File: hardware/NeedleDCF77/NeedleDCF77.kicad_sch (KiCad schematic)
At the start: 72 parts, among them J1 USB_C_Receptacle_USB2.0

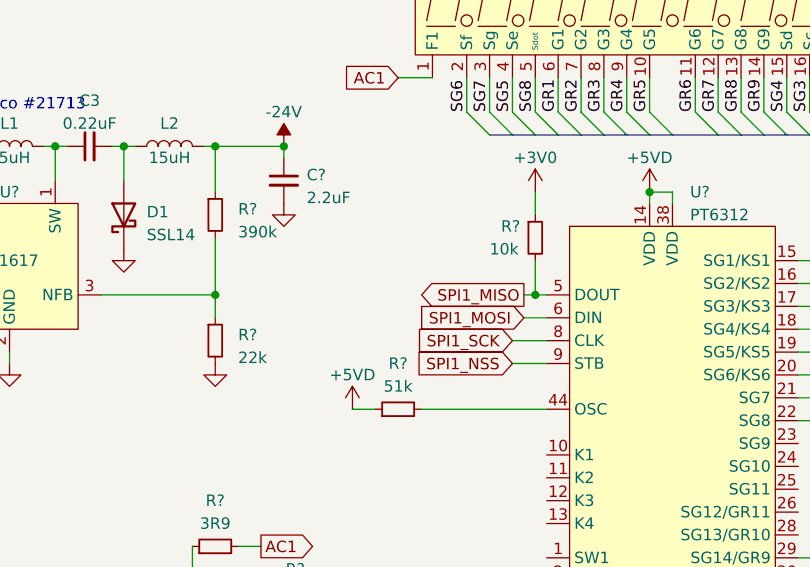
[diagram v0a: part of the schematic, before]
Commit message: Add solder jumper between Dout and Din for PT6312
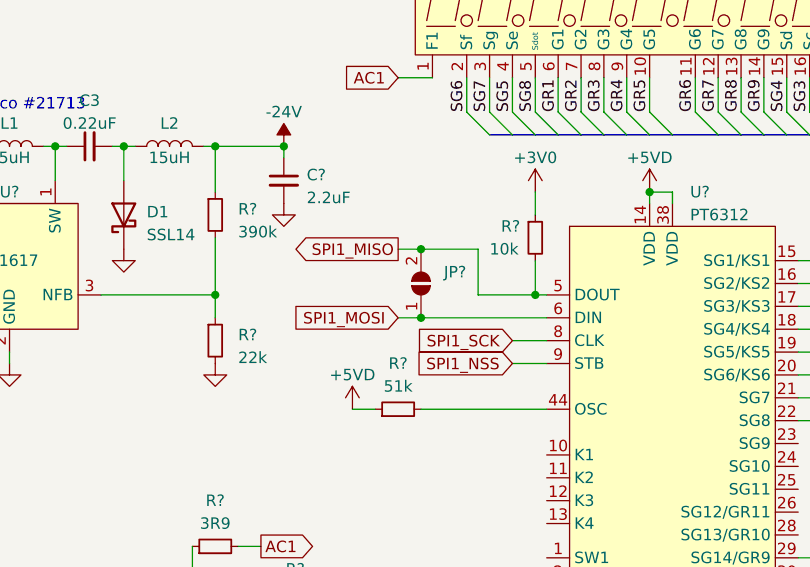
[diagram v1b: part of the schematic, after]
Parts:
- added JP?: (no value), symbol Jumper:SolderJumper_2_Open
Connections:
- net SPI1_MISO: now also JP?.2 (B)
- net SPI1_MOSI: now also JP?.1 (A)
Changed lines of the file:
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@@
   (junction (at 60.96 133.35) (diameter 0) (color 0 0 0 0)
   )
+  (junction (at 96.52 133.35) (diameter 0) (color 0 0 0 0)
+  )
   (junction (at 189.23 36.83) (diameter 0) (color 0 0 0 0)
   )
@@
   (junction (at 147.32 62.23) (diameter 0) (color 0 0 0 0)
   )
-  (junction (at 96.52 133.35) (diameter 0) (color 0 0 0 0)
-  )
   (junction (at 284.48 113.03) (diameter 0) (color 0 0 0 0)
   )
@@
   (junction (at 255.27 58.42) (diameter 0) (color 0 0 0 0)
   )
+  (junction (at 83.82 128.27) (diameter 0) (color 0 0 0 0)
+  )
   (junction (at 203.2 71.12) (diameter 0) (color 0 0 0 0)
   )
@@
   (junction (at 34.29 116.84) (diameter 0) (color 0 0 0 0)
   )
+  (junction (at 83.82 135.89) (diameter 0) (color 0 0 0 0)
+  )
   (junction (at 58.42 185.42) (diameter 0) (color 0 0 0 0)
   )
@@
     (stroke (width 0) (type default))
   )
+  (wire (pts (xy 90.17 128.27) (xy 90.17 133.35))
+    (stroke (width 0) (type default))
+  )
   (wire (pts (xy 284.48 110.49) (xy 284.48 113.03))
     (stroke (width 0) (type default))
@@
     (stroke (width 0) (type default))
   )
+  (wire (pts (xy 81.28 128.27) (xy 83.82 128.27))
+    (stroke (width 0) (type default))
+  )
   (wire (pts (xy 299.72 74.93) (xy 303.53 74.93))
     (stroke (width 0) (type default))
@@
     (stroke (width 0) (type default))
   )
-  (wire (pts (xy 95.25 133.35) (xy 96.52 133.35))
-    (stroke (width 0) (type default))
-  )
   (wire (pts (xy 147.32 62.23) (xy 152.4 62.23))
     (stroke (width 0) (type default))
@@
     (stroke (width 0) (type default))
   )
-  (wire (pts (xy 95.25 135.89) (xy 97.79 135.89))
+  (wire (pts (xy 81.28 135.89) (xy 83.82 135.89))
     (stroke (width 0) (type default))
   )
@@
     (stroke (width 0) (type default))
   )
+  (wire (pts (xy 83.82 135.89) (xy 97.79 135.89))
+    (stroke (width 0) (type default))
+  )
   (wire (pts (xy 111.76 123.19) (xy 111.76 121.92))
     (stroke (width 0) (type default))
@@
     (stroke (width 0) (type default))
   )
+  (wire (pts (xy 90.17 133.35) (xy 96.52 133.35))
+    (stroke (width 0) (type default))
+  )
   (wire (pts (xy 22.86 189.23) (xy 22.86 186.69))
     (stroke (width 0) (type default))
@@
     (stroke (width 0) (type default))
   )
+  (wire (pts (xy 83.82 128.27) (xy 90.17 128.27))
+    (stroke (width 0) (type default))
+  )
   (wire (pts (xy 152.4 41.91) (xy 128.27 41.91))
     (stroke (width 0) (type default))
@@
     )
   )
-  (global_label "SPI1_MOSI" (shape input) (at 95.25 135.89 180) (fields_autoplaced)
+  (global_label "SPI1_MOSI" (shape input) (at 81.28 135.89 180) (fields_autoplaced)
     (effects (font (size 1.27 1.27)) (justify right))
-    (property "Intersheetrefs" "${INTERSHEET_REFS}" (at 82.4866 135.89 0)
+    (property "Intersheetrefs" "${INTERSHEET_REFS}" (at 68.5166 135.89 0)
       (effects (font (size 1.27 1.27)) (justify right) hide)
     )
@@
     )
   )
-  (global_label "SPI1_MISO" (shape output) (at 95.25 133.35 180) (fields_autoplaced)
+  (global_label "SPI1_MISO" (shape output) (at 81.28 128.27 180) (fields_autoplaced)
     (effects (font (size 1.27 1.27)) (justify right))
-    (property "Intersheetrefs" "${INTERSHEET_REFS}" (at 82.4866 133.35 0)
+    (property "Intersheetrefs" "${INTERSHEET_REFS}" (at 68.5166 128.27 0)
       (effects (font (size 1.27 1.27)) (justify right) hide)
     )
@@
         )
       )
+    )
+  )
+  (symbol (lib_id "Jumper:SolderJumper_2_Open") (at 83.82 132.08 90) (unit 1)
+    (in_bom yes) (on_board yes) (dnp no)
+    (property "Reference" "JP?" (at 86.36 130.81 90)
+      (effects (font (size 1.27 1.27)) (justify right))
+    )
+    (property "Value" "" (at 72.39 132.08 90)
+      (effects (font (size 1.27 1.27)) (justify right))
+    )
+    (property "Footprint" "" (at 83.82 132.08 0)
+      (effects (font (size 1.27 1.27)) hide)
+    )
+    (property "Datasheet" "~" (at 83.82 132.08 0)
+      (effects (font (size 1.27 1.27)) hide)
+    )
+    (pin "1")
+    (pin "2")
+    (instances
+      (project "NeedleDCF77"
+        (path "/9538e4ed-27e6-4c37-b989-9859dc0d49e8"
+          (reference "JP?") (unit 1)
+        )
+      )

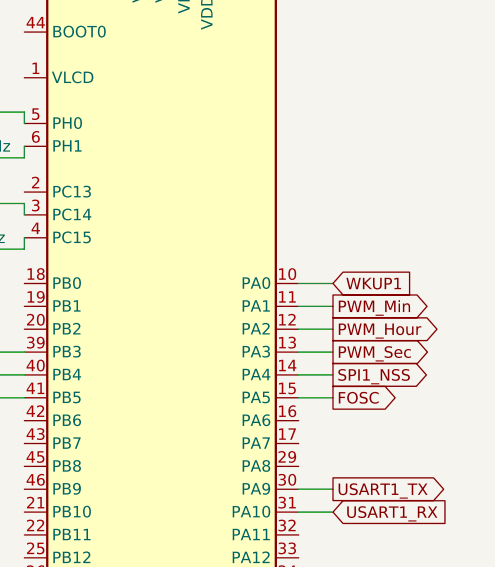
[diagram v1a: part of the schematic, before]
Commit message: Change WKUP to EXTI0, so we are unable to get out of LowPower modes, no STOP
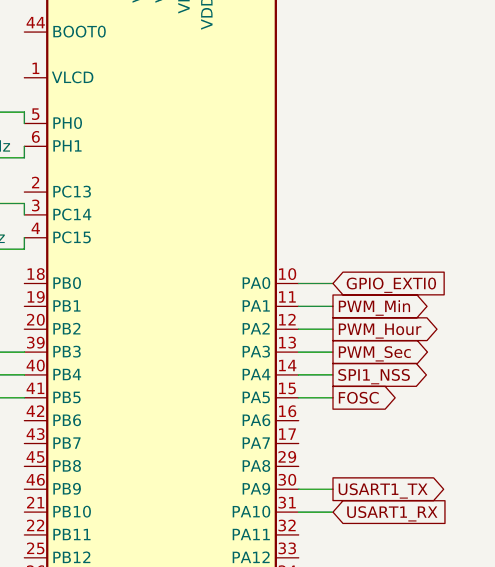
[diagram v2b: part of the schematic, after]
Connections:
- net WKUP1 renamed GPIO_EXTI0
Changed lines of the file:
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@@
     )
   )
-  (global_label "WKUP1" (shape input) (at 303.53 67.31 0) (fields_autoplaced)
+  (global_label "GPIO_EXTI0" (shape input) (at 303.53 67.31 0) (fields_autoplaced)
     (effects (font (size 1.27 1.27)) (justify left))
-    (property "Intersheetrefs" "${INTERSHEET_REFS}" (at 312.4745 67.2306 0)
+    (property "Intersheetrefs" "${INTERSHEET_REFS}" (at 317.0191 67.31 0)
       (effects (font (size 1.27 1.27)) (justify left) hide)
     )

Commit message: Add debug interfaces
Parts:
- added D?: CD4148W, Diode_SMD:D_0805_2012Metric, symbol Diode:CD4148W
- added J?: UART, symbol Connector:Conn_01x03_Pin
- added J?: DSW, symbol Connector:Conn_01x04_Pin
- JP?: value (none) -> ~
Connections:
- net +3V0: now also D?.1 (K)
- net GND: now also J?.1 (Pin_1), J?.3 (Pin_3)
- net SWCLK: now also J?.2 (Pin_2)
- net SWDIO: now also J?.3 (Pin_3)
- net USART1_RX: now also J?.1 (Pin_1)
- net USART1_TX: now also J?.2 (Pin_2)
- new net: D?.2 (A), J?.4 (Pin_4)
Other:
- moved on the sheet: C?, J?, JP?, R?, RV?, U?, VFD?

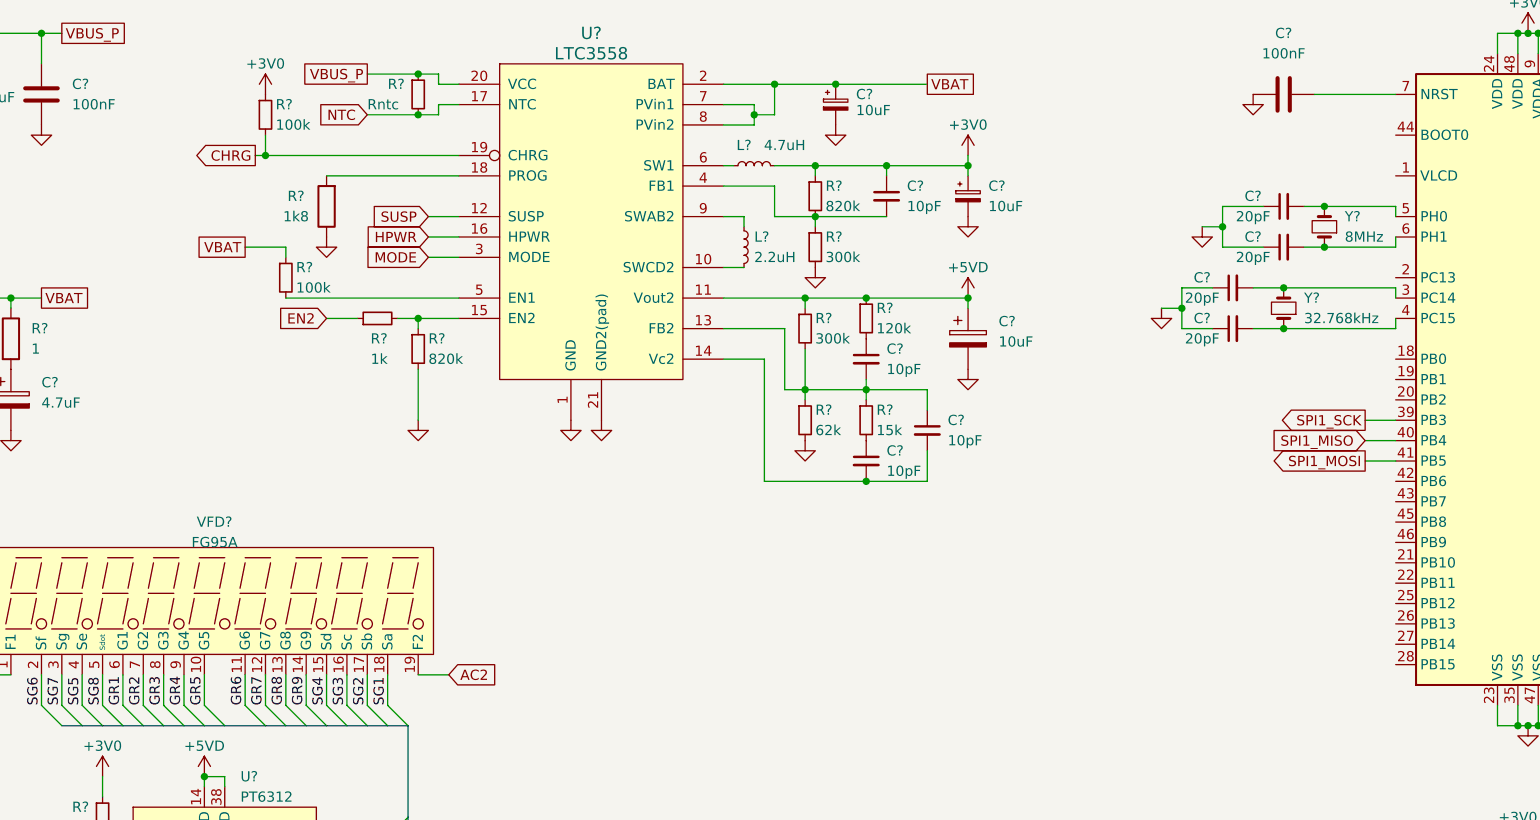
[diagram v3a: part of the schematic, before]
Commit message: Connect LTC3558 logic to MCU
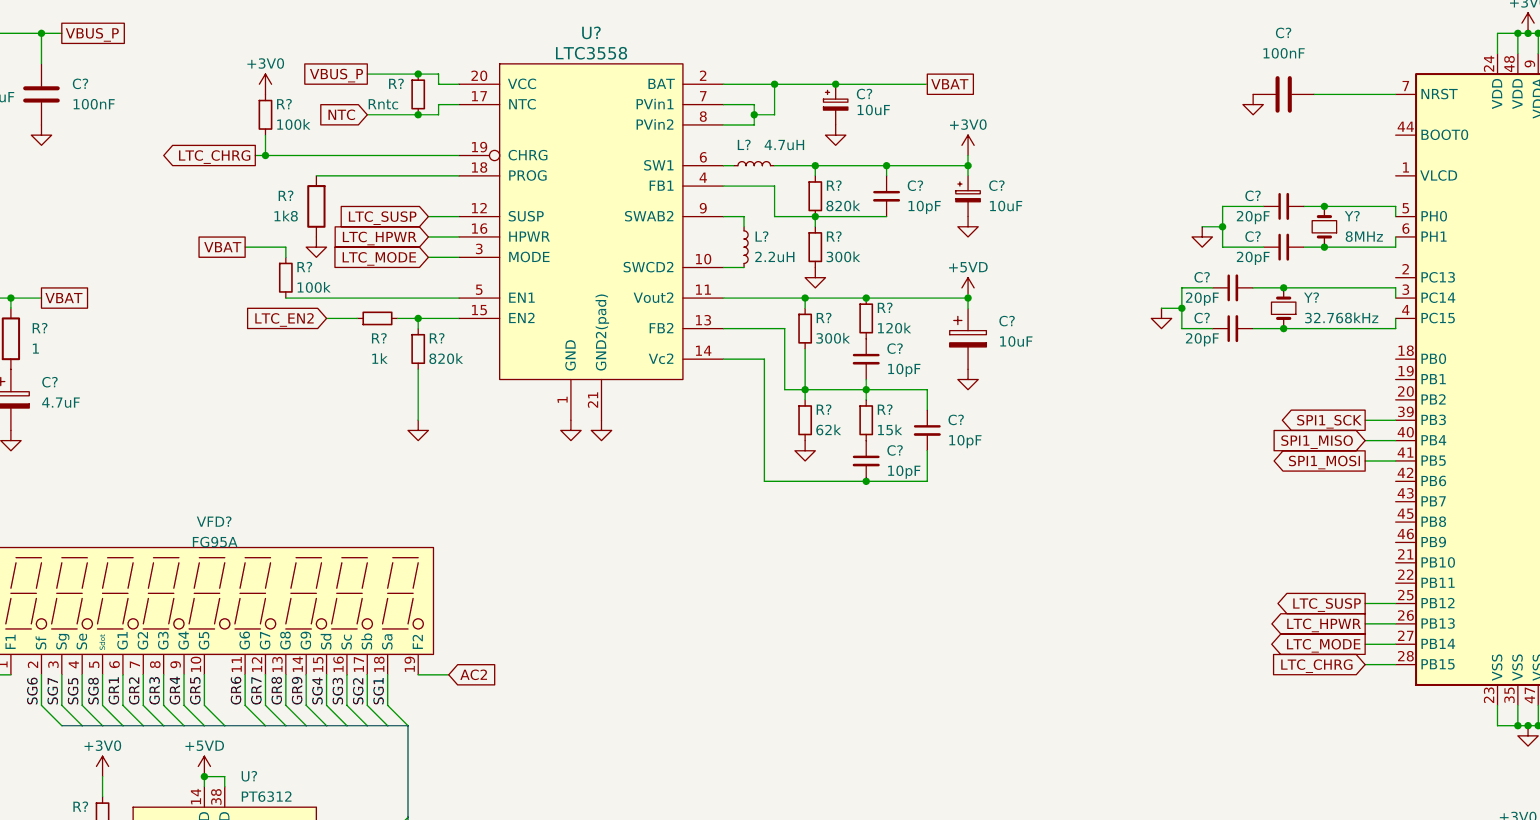
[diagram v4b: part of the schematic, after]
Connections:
- net CHRG is gone; now on net LTC_CHRG: R?.2, U?.19 (CHRG)
- net HPWR is gone; now on net LTC_HPWR: U?.16 (HPWR)
- net MODE is gone; now on net LTC_MODE: U?.3 (MODE)
- net SUSP is gone; now on net LTC_SUSP: U?.12 (SUSP)
- net LTC_SUSP: now reaches U?.25 (PB12)
- net LTC_HPWR: now reaches U?.26 (PB13)
- net LTC_MODE: now reaches U?.27 (PB14)
- net LTC_CHRG: now reaches U?.28 (PB15)
- net EN2 renamed LTC_EN2
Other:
- moved on the sheet: R?
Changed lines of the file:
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@@
+    (stroke (width 0) (type default))
+  )
+  (wire (pts (xy 265.43 100.33) (xy 269.24 100.33))
     (stroke (width 0) (type default))
   )
@@
     (stroke (width 0) (type default))
   )
+  (wire (pts (xy 265.43 105.41) (xy 269.24 105.41))
+    (stroke (width 0) (type default))
+  )
   (wire (pts (xy 58.42 185.42) (xy 58.42 193.04))
     (stroke (width 0) (type default))
@@
     (stroke (width 0) (type default))
   )
+  (wire (pts (xy 265.43 97.79) (xy 269.24 97.79))
+    (stroke (width 0) (type default))
+  )
   (wire (pts (xy 149.86 33.02) (xy 149.86 31.75))
     (stroke (width 0) (type default))
@@
     (stroke (width 0) (type default))
   )
-  (wire (pts (xy 135.89 44.45) (xy 152.4 44.45))
+  (wire (pts (xy 134.62 44.45) (xy 152.4 44.45))
     (stroke (width 0) (type default))
   )
@@
     (stroke (width 0) (type default))
   )
+  (wire (pts (xy 265.43 102.87) (xy 269.24 102.87))
+    (stroke (width 0) (type default))
+  )
   (wire (pts (xy 149.86 35.56) (xy 149.86 36.83))
     (stroke (width 0) (type default))
@@
     (effects (font (size 1.27 1.27)) (justify left bottom))
   )
-  (global_label "CHRG" (shape output) (at 127 41.91 180) (fields_autoplaced)
-    (effects (font (size 1.27 1.27)) (justify right))
-    (property "Intersheetrefs" "${INTERSHEET_REFS}" (at 119.4464 41.8306 0)
+  (global_label "LTC_CHRG" (shape output) (at 127 41.91 180) (fields_autoplaced)
+    (effects (font (size 1.27 1.27)) (justify right))
+    (property "Intersheetrefs" "${INTERSHEET_REFS}" (at 114.7204 41.91 0)
       (effects (font (size 1.27 1.27)) (justify right) hide)
     )
@@
     )
   )
+  (global_label "LTC_HPWR" (shape output) (at 265.43 100.33 180) (fields_autoplaced)
+    (effects (font (size 1.27 1.27)) (justify right))
+    (property "Intersheetrefs" "${INTERSHEET_REFS}" (at 252.969 100.33 0)
+      (effects (font (size 1.27 1.27)) (justify right) hide)
+    )
+  )
   (global_label "NTC" (shape output) (at 87.63 62.23 0) (fields_autoplaced)
     (effects (font (size 1.27 1.27)) (justify left))
@@
     )
   )
-  (global_label "HPWR" (shape input) (at 148.59 52.07 180) (fields_autoplaced)
-    (effects (font (size 1.27 1.27)) (justify right))
-    (property "Intersheetrefs" "${INTERSHEET_REFS}" (at 140.855 51.9906 0)
+  (global_label "LTC_HPWR" (shape input) (at 148.59 52.07 180) (fields_autoplaced)
+    (effects (font (size 1.27 1.27)) (justify right))
+    (property "Intersheetrefs" "${INTERSHEET_REFS}" (at 136.129 52.07 0)
+      (effects (font (size 1.27 1.27)) (justify right) hide)
+    )
+  )
+  (global_label "LTC_CHRG" (shape input) (at 265.43 105.41 180) (fields_autoplaced)
+    (effects (font (size 1.27 1.27)) (justify right))
+    (property "Intersheetrefs" "${INTERSHEET_REFS}" (at 253.1504 105.41 0)
       (effects (font (size 1.27 1.27)) (justify right) hide)
     )
@@
     )
   )
+  (global_label "LTC_SUSP" (shape output) (at 265.43 97.79 180) (fields_autoplaced)
+    (effects (font (size 1.27 1.27)) (justify right))
+    (property "Intersheetrefs" "${INTERSHEET_REFS}" (at 253.2714 97.79 0)
+      (effects (font (size 1.27 1.27)) (justify right) hide)
+    )
+  )
   (global_label "USART1_RX" (shape output) (at 292.1 148.59 180) (fields_autoplaced)
     (effects (font (size 1.27 1.27)) (justify right))
@@
     )
   )
-  (global_label "SUSP" (shape input) (at 148.59 49.53 180) (fields_autoplaced)
-    (effects (font (size 1.27 1.27)) (justify right))
-    (property "Intersheetrefs" "${INTERSHEET_REFS}" (at 141.1574 49.4506 0)
+  (global_label "LTC_MODE" (shape output) (at 265.43 102.87 180) (fields_autoplaced)
+    (effects (font (size 1.27 1.27)) (justify right))
+    (property "Intersheetrefs" "${INTERSHEET_REFS}" (at 253.09 102.87 0)
+      (effects (font (size 1.27 1.27)) (justify right) hide)
+    )
+  )
+  (global_label "LTC_SUSP" (shape input) (at 148.59 49.53 180) (fields_autoplaced)
+    (effects (font (size 1.27 1.27)) (justify right))
+    (property "Intersheetrefs" "${INTERSHEET_REFS}" (at 136.4314 49.53 0)
       (effects (font (size 1.27 1.27)) (justify right) hide)
     )
@@
     )
   )
-  (global_label "MODE" (shape input) (at 148.59 54.61 180) (fields_autoplaced)
-    (effects (font (size 1.27 1.27)) (justify right))
-    (property "Intersheetrefs" "${INTERSHEET_REFS}" (at 140.9759 54.5306 0)
+  (global_label "LTC_MODE" (shape input) (at 148.59 54.61 180) (fields_autoplaced)
+    (effects (font (size 1.27 1.27)) (justify right))
+    (property "Intersheetrefs" "${INTERSHEET_REFS}" (at 136.25 54.61 0)
       (effects (font (size 1.27 1.27)) (justify right) hide)
     )
@@
     )
   )
-  (global_label "EN2" (shape input) (at 135.89 62.23 180) (fields_autoplaced)
-    (effects (font (size 1.27 1.27)) (justify right))
-    (property "Intersheetrefs" "${INTERSHEET_REFS}" (at 129.7879 62.1506 0)
+  (global_label "LTC_EN2" (shape input) (at 135.89 62.23 180) (fields_autoplaced)
+    (effects (font (size 1.27 1.27)) (justify right))
+    (property "Intersheetrefs" "${INTERSHEET_REFS}" (at 125.0619 62.23 0)
       (effects (font (size 1.27 1.27)) (justify right) hide)
     )
@@
     )
   )
-  (symbol (lib_id "power:GND") (at 135.89 52.07 0) (unit 1)
+  (symbol (lib_id "power:GND") (at 134.62 52.07 0) (unit 1)
     (in_bom yes) (on_board yes) (dnp no) (fields_autoplaced)
-    (property "Reference" "#PWR0116" (at 135.89 58.42 0)
-      (effects (font (size 1.27 1.27)) hide)
-    )
-    (property "Value" "GND" (at 135.89 57.15 0)
-      (effects (font (size 1.27 1.27)) hide)
-    )
-    (property "Footprint" "" (at 135.89 52.07 0)
-      (effects (font (size 1.27 1.27)) hide)
-    )
-    (property "Datasheet" "" (at 135.89 52.07 0)
+    (property "Reference" "#PWR0116" (at 134.62 58.42 0)
+      (effects (font (size 1.27 1.27)) hide)
+    )
+    (property "Value" "GND" (at 134.62 57.15 0)
+      (effects (font (size 1.27 1.27)) hide)
+    )
+    (property "Footprint" "" (at 134.62 52.07 0)
+      (effects (font (size 1.27 1.27)) hide)
+    )
+    (property "Datasheet" "" (at 134.62 52.07 0)
       (effects (font (size 1.27 1.27)) hide)
     )
@@
     )
   )
-  (symbol (lib_id "Device:R") (at 135.89 48.26 180) (unit 1)
+  (symbol (lib_id "Device:R") (at 134.62 48.26 180) (unit 1)
     (in_bom yes) (on_board yes) (dnp no)
-    (property "Reference" "R?" (at 132.08 46.99 0)
+    (property "Reference" "R?" (at 130.81 46.99 0)
       (effects (font (size 1.27 1.27)))
     )
-    (property "Value" "1k8" (at 132.08 49.53 0)
+    (property "Value" "1k8" (at 130.81 49.53 0)
       (effects (font (size 1.27 1.27)))
     )
-    (property "Footprint" "" (at 137.668 48.26 90)
-      (effects (font (size 1.27 1.27)) hide)
-    )
-    (property "Datasheet" "~" (at 135.89 48.26 0)
-      (effects (font (size 1.27 1.27)) hide)
-    )
+    (property "Footprint" "" (at 136.398 48.26 90)
+      (effects (font (size 1.27 1.27)) hide)
+    )
+    (property "Datasheet" "~" (at 134.62 48.26 0)
+      (effects (font (size 1.27 1.27)) hide)
+    )
